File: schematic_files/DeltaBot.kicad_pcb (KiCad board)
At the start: 2 copper layers, 241.5 x 110.5 mm, 30 parts, among them J1 USB C PD Modulle, J2 LIDAR, J3 MOTOR_L, J4 MOTOR_R, SW1 SW_SPDT, U1 Radxa_ROCK5B, U2 Buck Converter

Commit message: Updated PCB layout
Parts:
- removed D1, D2: D, deltabot:D_DO-41_SOD81_P10.16mm_Horizontal
- removed REF** (x13), REF\: MountingHole_3.5mm, MountingHole:MountingHole_3.5mm
- J2: value LIDAR -> Conn_01x05; footprint deltabot:PinHeader_1x07_P2.54mm_Vertical -> Connector_PinHeader_2.54mm:PinHeader_1x05_P2.54mm_Vertical
- moved C1 191.3 mm to (40.5, 99.5)
- moved C2 176.7 mm to (43.2, 87.0), turned to 0 degrees
- moved U2 146.3 mm to (83.0, 100.5), turned to 180 degrees
- moved J2 5.07 mm to (171.1, 60.5)
- turned SW1 to 0 degrees
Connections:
- J2 pad 1: Net-(D2-K) -> unconnected-(J2-Pin_1-Pad1)
- J2 pad 2: MOTO_CTRL -> +5V
- J2 pad 3: GND -> LIDAR_TX
- J2 pad 4: +5V -> LIDAR_RX
- J2 pad 5: LIDAR_TX -> GND
- U1 pad 10: LIDAR_RX -> LIDAR_TX
- U1 pad 8: LIDAR_TX -> LIDAR_RX
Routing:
- net MOTO_CTRL: track 99.9 -> 0.00 mm, vias 1 -> 0
- net +5V: track 329.1 -> 380.8 mm
- net +9V: track 65.3 -> 113.4 mm
- net Net-(D2-K): track 35.8 -> 0.00 mm
- net LIDAR_TX: track 128.5 -> 105.5 mm
- net PWM_L: track 124.7 -> 140.5 mm
- net GND: track 11.4 -> 0.00 mm
- net Net-(D1-K): track 5.92 -> 0.00 mm
- net LIDAR_RX: track 112.6 -> 115.9 mm
- net Net-(SW1-B): track 72.0 -> 72.6 mm

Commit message: Small changes
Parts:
- moved J2 2.50 mm to (168.6, 60.5)
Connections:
- J2 pad 1: unconnected-(J2-Pin_1-Pad1) -> +5V
- J2 pad 2: +5V -> LIDAR_TX
- J2 pad 3: LIDAR_TX -> LIDAR_RX
- J2 pad 4: LIDAR_RX -> GND
- J2 pad 5: GND -> unconnected-(J2-Pin_5-Pad5)
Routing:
- net +5V: track 380.8 -> 375.9 mm
- net LIDAR_RX: track 115.9 -> 116.4 mm
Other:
- board text removed: "LIDAR_RX"
- board text removed: "LIDAR_TX"
- board text removed: "MOTOR_CTRL"
- board text removed: "PWM_R"
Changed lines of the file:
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@@
 	(net 34 "unconnected-(U1-GPIO2_B3-Pad7)")
 	(net 35 "PWM_R")
-	(net 36 "unconnected-(J2-Pin_1-Pad1)")
+	(net 36 "unconnected-(J2-Pin_5-Pad5)")
 	(net 37 "+9V")
 	(footprint "deltabot:C_Disc_D3.0mm_W2.0mm_P2.50mm"
@@
 			)
 		)
-		(group ""
-			(members "633756a8-9496-4de9-8571-4000073fd013" "c9b2ae1b-2e5a-42f9-9f94-d1d775f59a72")
-		)
 		(embedded_fonts no)
 	)
 	(footprint "Connector_PinHeader_2.54mm:PinHeader_1x05_P2.54mm_Vertical"
 		(layer "F.Cu")
-		(at 171.08 60.5 -90)
+		(at 168.58 60.5 -90)
 		(descr "Through hole straight pin header, 1x05, 2.54mm pitch, single row")
 		(tags "Through hole pin header THT 1x05 2.54mm single row")
@@
 			(layers "*.Cu" "*.Mask")
 			(remove_unused_layers no)
-			(net 36 "unconnected-(J2-Pin_1-Pad1)")
+			(net 26 "+5V")
 			(pinfunction "Pin_1")
 			(pintype "passive")
@@
 			(layers "*.Cu" "*.Mask")
 			(remove_unused_layers no)
-			(net 26 "+5V")
+			(net 10 "LIDAR_TX")
 			(pinfunction "Pin_2")
 			(pintype "passive")
@@
 			(layers "*.Cu" "*.Mask")
 			(remove_unused_layers no)
-			(net 10 "LIDAR_TX")
+			(net 27 "LIDAR_RX")
 			(pinfunction "Pin_3")
 			(pintype "passive")
@@
 			(layers "*.Cu" "*.Mask")
 			(remove_unused_layers no)
-			(net 27 "LIDAR_RX")
+			(net 1 "GND")
 			(pinfunction "Pin_4")
 			(pintype "passive")
@@
 			(layers "*.Cu" "*.Mask")
 			(remove_unused_layers no)
-			(net 1 "GND")
+			(net 36 "unconnected-(J2-Pin_5-Pad5)")
 			(pinfunction "Pin_5")
 			(pintype "passive")
@@
 		)
 	)
-	(gr_text "LIDAR_TX\n"
-		(at 114 45 0)
-		(layer "User.4")
-		(effects
-			(font
-				(size 1.5 1.5)
-				(thickness 0.3)
-				(bold yes)
-			)
-			(justify left bottom)
-		)
-	)
-	(gr_text "LIDAR_RX\n"
-		(at 114 55 0)
-		(layer "User.4")
-		(effects
-			(font
-				(size 1.5 1.5)
-				(thickness 0.3)
-				(bold yes)
-			)
-			(justify left bottom)
-		)
-	)
-	(gr_text "MOTOR_CTRL\n"
-		(at 114 66 0)
-		(layer "User.4")
-		(effects
-			(font
-				(size 1.5 1.5)
-				(thickness 0.3)
-				(bold yes)
-			)
-			(justify left bottom)
-		)
-	)
 	(gr_text "+9V"
 		(at 170 114 0)
@@
 		)
 	)
-	(gr_text "PWM_R"
-		(at 114 69 0)
-		(layer "User.8")
-		(effects
-			(font
-				(size 1.5 1.5)
-				(thickness 0.3)
-				(bold yes)
-			)
-			(justify left bottom)
-		)
-	)
 	(gr_text "PWM_L\n"
 		(at 132.5 110 0)
@@
 	)
 	(via
-		(at 156 60)
+		(at 153.5 60.5)
 		(size 2.5)
 		(drill 1)
@@
 	)
 	(via
-		(at 179.5 58)
+		(at 180 55)
 		(size 2.5)
 		(drill 1)
@@
 	)
 	(via
-		(at 77 68)
+		(at 77 69.5)
 		(size 2.5)
 		(drill 1)
@@
 	)
 	(via
-		(at 96.5 79.5)
+		(at 92.5 79.5)
 		(size 2.5)
 		(drill 1)
@@
 	)
 	(segment
+		(start 166.04 60.5)
+		(end 166 60.5)
+		(width 0.5)
+		(layer "B.Cu")
+		(net 10)
+	)
+	(segment
 		(start 166 63.5)
 		(end 166 60.5)
@@
 	)
 	(segment
-		(start 58.5 60)
-		(end 58.5 55)
-		(width 1)
+		(start 186.5 40.5)
+		(end 201 55)
+		(width 2.5)
 		(layer "B.Cu")
 		(net 26)
 	)
 	(segment
-		(start 186.5 40.5)
-		(end 201 55)
-		(width 2.5)
+		(start 168.58 60.5)
+		(end 168.58 60.075)
+		(width 0.5)
 		(layer "B.Cu")
 		(net 26)
 	)
 	(segment
-		(start 209 62)
-		(end 209 114.5)
-		(width 2)
+		(start 168.58 60.075)
+		(end 168.505 60)
+		(width 0.5)
 		(layer "B.Cu")
 		(net 26)
 	)
 	(segment
-		(start 60 53.5)
-		(end 64 53.5)
-		(width 1)
+		(start 209 62)
+		(end 209 114.5)
+		(width 2)
 		(layer "B.Cu")
 		(net 26)
@@
 	)
 	(segment
+		(start 58.5 60)
+		(end 63.5 60)
+		(width 1)
+		(layer "B.Cu")
+		(net 26)
+	)
+	(segment
 		(start 207.04 63.96)
 		(end 205.25 63.96)
@@
 	)
 	(segment
-		(start 58.5 55)
-		(end 60 53.5)
-		(width 1)
-		(layer "B.Cu")
-		(net 26)
-	)
-	(segment
 		(start 209 114.5)
 		(end 206.46 117.04)
@@
 	)
 	(segment
+		(start 63.5 60)
+		(end 64 59.5)
+		(width 1)
+		(layer "B.Cu")
+		(net 26)
+	)
+	(segment
 		(start 202.75 71.75)
 		(end 205.25 69.25)
@@
 	)
 	(segment
-		(start 124.5 59.5)
-		(end 130 54)
+		(start 130 54)
+		(end 163.5 54)
 		(width 1)
 		(layer "B.Cu")
@@
 	)
 	(segment
-		(start 163.5 54)
-		(end 163.5 60)
+		(start 124.5 59.5)
+		(end 130 54)
 		(width 1)
 		(layer "B.Cu")
@@
 	)
 	(segment
-		(start 130 54)
-		(end 163.5 54)
+		(start 163.5 54)
+		(end 163.5 60.5)
 		(width 1)
 		(layer "B.Cu")

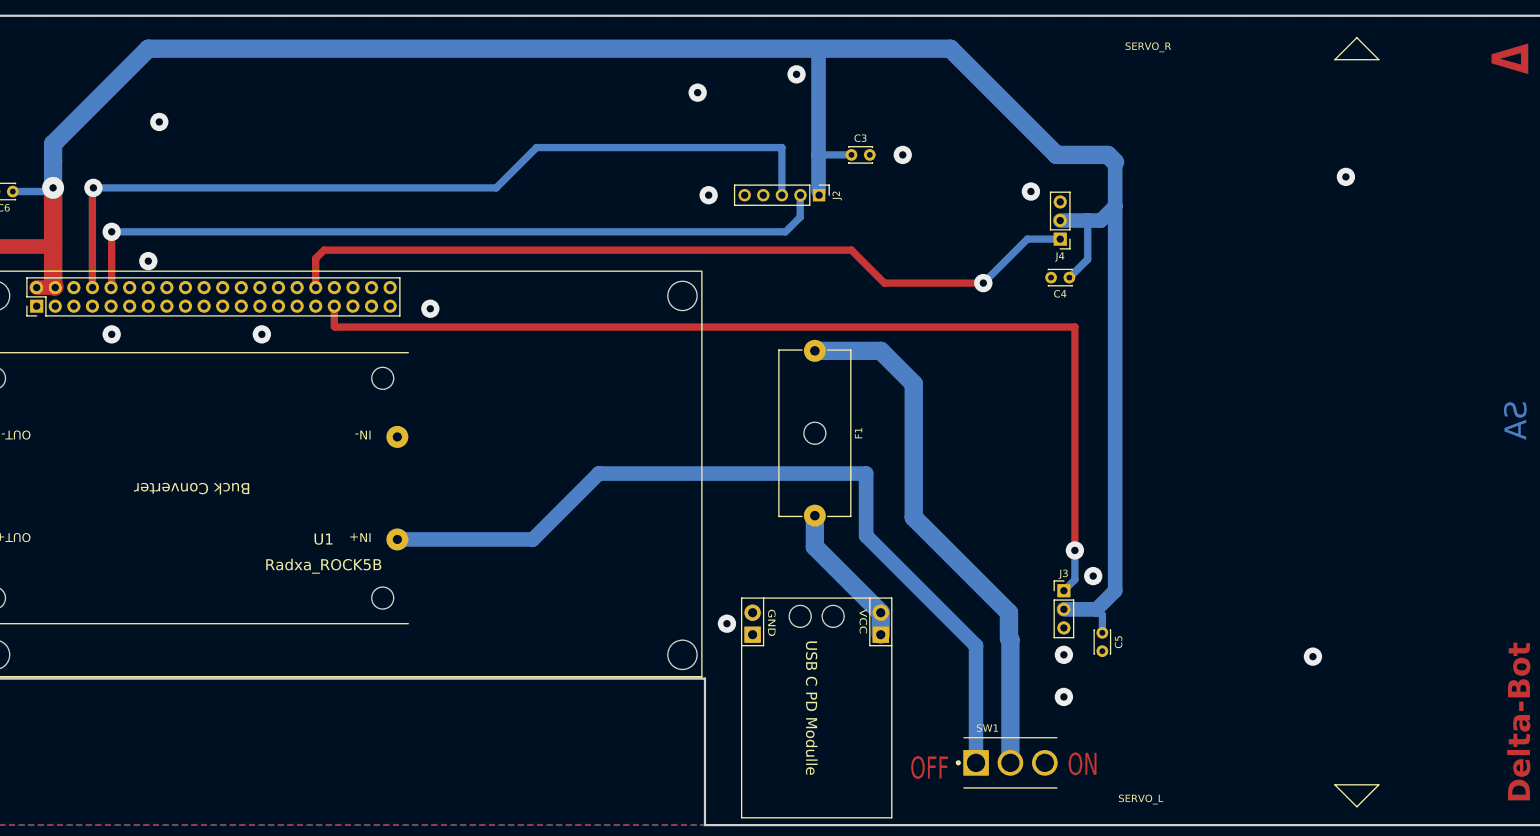
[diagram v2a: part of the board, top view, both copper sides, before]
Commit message: Added C1 LIDAR to the footprints.
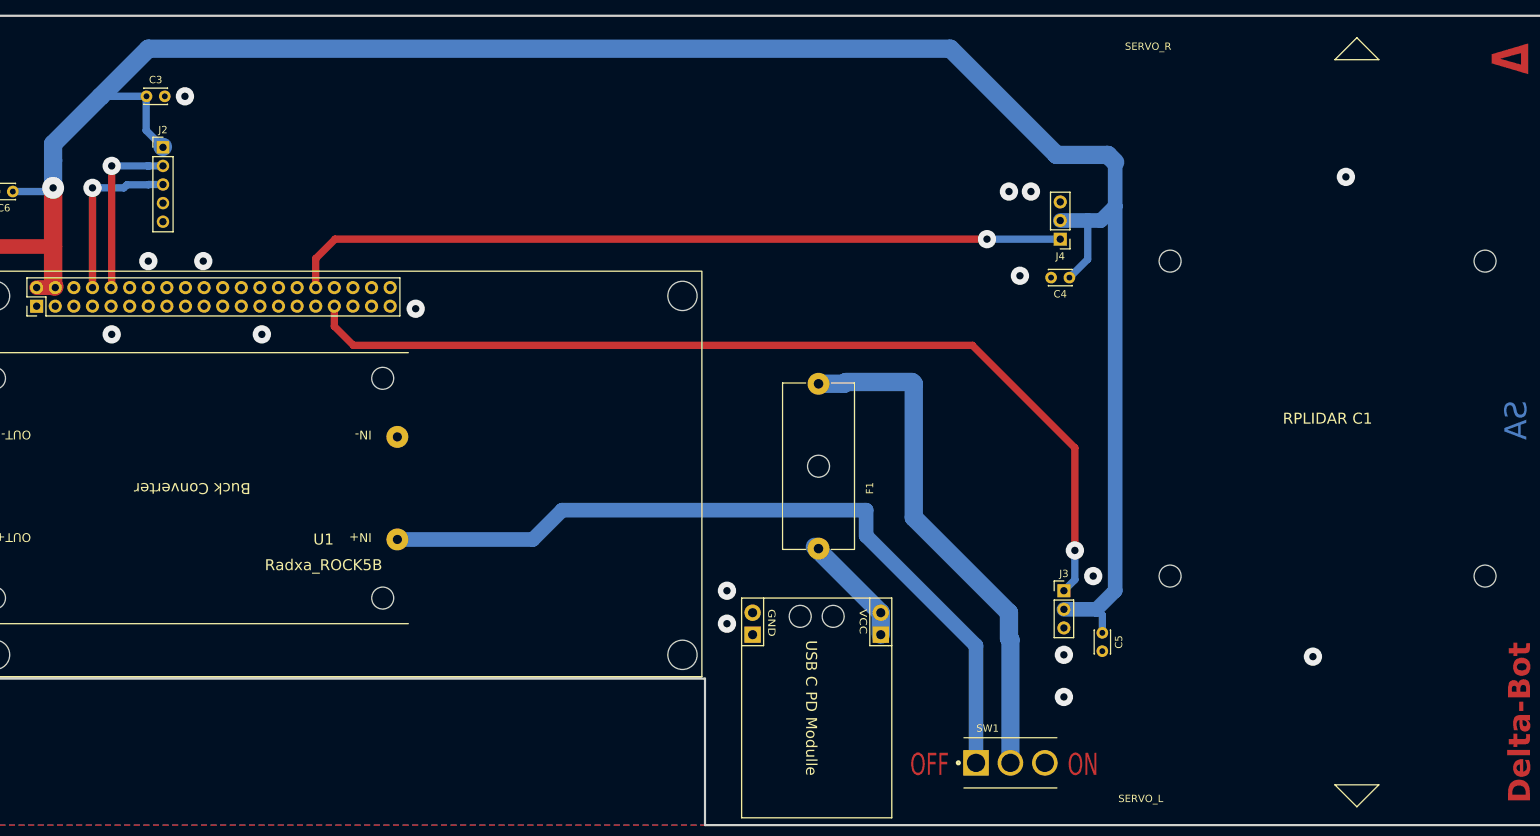
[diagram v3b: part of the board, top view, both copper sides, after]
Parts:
- added U1: RPLIDAR C1, deltabot:RPLIDAR C1, F.Cu at (238.0, 91.0)
- J2: value Conn_01x05 -> LIDAR
- moved C3 96.6 mm to (76.8, 47.0)
- moved J2 89.8 mm to (79.0, 54.0), turned to 0 degrees
- moved F1 4.53 mm to (168.5, 86.2)
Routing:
- net LIDAR_RX: track 116.4 -> 23.4 mm
- net LIDAR_TX: track 105.5 -> 23.7 mm
- net PWM_L: track 140.5 -> 130.8 mm
- net +5V: track 375.9 -> 366.3 mm
- net +9V: track 113.4 -> 106.4 mm
- net Net-(J1-VCC): track 20.0 -> 15.7 mm
- net PWM_R: track 110.4 -> 106.7 mm
- net Net-(SW1-B): track 72.6 -> 70.4 mm
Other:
- board text removed: "+5V"
- board text removed: "+8.34V"
- board text removed: "+9V"
- board text removed: "PWM_L"

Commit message: Fixed the Rock5B footprint which was slightly off.
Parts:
- moved U1 0.84 mm to (101.8, 109.0)
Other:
- outline, holes or cut-outs redrawn

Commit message: Added files for GU manufacture
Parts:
- moved C5 8.61 mm to (199.5, 124.0), turned to 0 degrees
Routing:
- net +5V: track 366.3 -> 372.2 mm
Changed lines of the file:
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@@
 		(1 "F.Mask" user)
 		(3 "B.Mask" user)
-		(17 "Dwgs.User" user "User.Drawings")
-		(19 "Cmts.User" user "User.Comments")
-		(21 "Eco1.User" user "User.Eco1")
-		(23 "Eco2.User" user "User.Eco2")
 		(25 "Edge.Cuts" user)
 		(27 "Margin" user)
@@
 		(35 "F.Fab" user)
 		(33 "B.Fab" user)
-		(39 "User.1" user)
-		(41 "User.2" user)
-		(43 "User.3" user)
-		(45 "User.4" user)
-		(47 "User.5" user)
-		(49 "User.6" user)
-		(51 "User.7" user)
-		(53 "User.8" user)
-		(55 "User.9" user)
 	)
 	(setup
+		(stackup
+			(layer "F.SilkS"
+				(type "Top Silk Screen")
+			)
+			(layer "F.Paste"
+				(type "Top Solder Paste")
+			)
+			(layer "F.Mask"
+				(type "Top Solder Mask")
+				(thickness 0.01)
+			)
+			(layer "F.Cu"
+				(type "copper")
+				(thickness 0.035)
+			)
+			(layer "dielectric 1"
+				(type "core")
+				(thickness 1.51)
+				(material "FR4")
+				(epsilon_r 4.5)
+				(loss_tangent 0.02)
+			)
+			(layer "B.Cu"
+				(type "copper")
+				(thickness 0.035)
+			)
+			(layer "B.Mask"
+				(type "Bottom Solder Mask")
+				(thickness 0.01)
+			)
+			(layer "B.Paste"
+				(type "Bottom Solder Paste")
+			)
+			(layer "B.SilkS"
+				(type "Bottom Silk Screen")
+			)
+			(copper_finish "None")
+			(dielectric_constraints no)
+		)
 		(pad_to_mask_clearance 0)
 		(allow_soldermask_bridges_in_footprints no)
@@
 			(drillshape 0)
 			(scaleselection 1)
-			(outputdirectory "../../pcb svg/new schem & pcb/")
+			(outputdirectory "/tmp/drill")
 		)
 	)
@@
 	(footprint "deltabot:C_Disc_D3.0mm_W2.0mm_P2.50mm"
 		(layer "F.Cu")
-		(at 207.25 120.25 -90)
+		(at 199.5 124)
 		(descr "C, Disc series, Radial, pin pitch=2.50mm, , diameter*width=3*2mm^2, Capacitor")
 		(tags "C Disc series Radial pin pitch 2.50mm  diameter 3mm width 2mm Capacitor")
 		(property "Reference" "C5"
-			(at 1.25 -2.25 90)
+			(at 1.25 -2.25 0)
 			(layer "F.SilkS")
 			(effects
@@
 		)
 		(property "Value" "1uF"
-			(at 1.25 2.25 90)
+			(at 1.25 2.25 0)
 			(layer "F.Fab")
 			(effects
@@
 		)
 		(property "Datasheet" "~"
-			(at 0 0 270)
+			(at 0 0 0)
 			(unlocked yes)
 			(layer "F.Fab")
@@
 		)
 		(property "Description" "Polarized capacitor"
-			(at 0 0 270)
+			(at 0 0 0)
 			(unlocked yes)
 			(layer "F.Fab")
@@
 		(attr through_hole)
 		(fp_line
-			(start -0.37 1.12)
-			(end 2.87 1.12)
+			(start -0.37 -1.12)
+			(end -0.37 -1.055)
 			(stroke
 				(width 0.12)
@@
 		)
 		(fp_line
-			(start -0.37 1.055)
-			(end -0.37 1.12)
+			(start -0.37 -1.12)
+			(end 2.87 -1.12)
 			(stroke
 				(width 0.12)
@@
 		)
 		(fp_line
-			(start 2.87 1.055)
-			(end 2.87 1.12)
+			(start -0.37 1.055)
+			(end -0.37 1.12)
 			(stroke
 				(width 0.12)
@@
 		)
 		(fp_line
-			(start -0.37 -1.12)
-			(end -0.37 -1.055)
+			(start -0.37 1.12)
+			(end 2.87 1.12)
 			(stroke
 				(width 0.12)
@@
 		)
 		(fp_line
-			(start -0.37 -1.12)
-			(end 2.87 -1.12)
+			(start 2.87 -1.12)
+			(end 2.87 -1.055)
 			(stroke
 				(width 0.12)
@@
 		)
 		(fp_line
-			(start 2.87 -1.12)
-			(end 2.87 -1.055)
+			(start 2.87 1.055)
+			(end 2.87 1.12)
 			(stroke
 				(width 0.12)
@@
 		)
 		(fp_line
-			(start -1.05 1.25)
-			(end 3.55 1.25)
+			(start -1.05 -1.25)
+			(end -1.05 1.25)
 			(stroke
 				(width 0.05)
@@
 		)
 		(fp_line
-			(start 3.55 1.25)
-			(end 3.55 -1.25)
+			(start -1.05 1.25)
+			(end 3.55 1.25)
 			(stroke
 				(width 0.05)
@@
 		)
 		(fp_line
-			(start -1.05 -1.25)
-			(end -1.05 1.25)
+			(start 3.55 -1.25)
+			(end -1.05 -1.25)
 			(stroke
 				(width 0.05)
@@
 		)
 		(fp_line
-			(start 3.55 -1.25)
-			(end -1.05 -1.25)
+			(start 3.55 1.25)
+			(end 3.55 -1.25)
 			(stroke
 				(width 0.05)
@@
 		)
 		(fp_line
-			(start -0.25 1)
-			(end 2.75 1)
+			(start -0.25 -1)
+			(end -0.25 1)
 			(stroke
 				(width 0.1)
@@
 		)
 		(fp_line
-			(start 2.75 1)
-			(end 2.75 -1)
+			(start -0.25 1)
+			(end 2.75 1)
 			(stroke
 				(width 0.1)
@@
 		)
 		(fp_line
-			(start -0.25 -1)
-			(end -0.25 1)
+			(start 2.75 -1)
+			(end -0.25 -1)
 			(stroke
 				(width 0.1)
@@
 		)
 		(fp_line
-			(start 2.75 -1)
-			(end -0.25 -1)
+			(start 2.75 1)
+			(end 2.75 -1)
 			(stroke
 				(width 0.1)
@@
 		)
 		(fp_text user "${REFERENCE}"
-			(at 1.25 0 90)
+			(at 1.25 0 0)
 			(layer "F.Fab")
 			(effects
@@
 		)
 		(pad "1" thru_hole circle
-			(at 0 0 270)
+			(at 0 0)
 			(size 1.6 1.6)
 			(drill 0.8)
@@
 		)
 		(pad "2" thru_hole circle
-			(at 2.5 0 270)
+			(at 2.5 0)
 			(size 1.6 1.6)
 			(drill 0.8)
@@
 	)
 	(gr_line
-		(start 208.5 50.5)
-		(end 208.5 37)
-		(stroke
-			(width 0.12)
-			(type solid)
-		)
-		(layer "Cmts.User")
-	)
-	(gr_line
-		(start 208.5 50.5)
-		(end 248.5 50.5)
-		(stroke
-			(width 0.12)
-			(type solid)
-		)
-		(layer "Cmts.User")
-	)
-	(gr_line
-		(start 208.5 132.5)
-		(end 208.5 145.5)
-		(stroke
-			(width 0.12)
-			(type solid)
-		)
-		(layer "Cmts.User")
-	)
-	(gr_line
-		(start 248.5 50.5)
-		(end 248.5 37)
-		(stroke
-			(width 0.12)
-			(type solid)
-		)
-		(layer "Cmts.User")
-	)
-	(gr_line
-		(start 248.5 132.5)
-		(end 208.5 132.5)
-		(stroke
-			(width 0.12)
-			(type solid)
-		)
-		(layer "Cmts.User")
-	)
-	(gr_line
-		(start 248.5 132.5)
-		(end 248.5 145.5)
-		(stroke
-			(width 0.12)
-			(type solid)
-		)
-		(layer "Cmts.User")
-	)
-	(gr_line
 		(start 27 36)
 		(end 268.5 36)
@@
 		)
 	)
-	(gr_text "\n"
-		(at 208 97.5 0)
-		(layer "Cmts.User")
-		(effects
-			(font
-				(size 1.5 1.5)
-				(thickness 0.3)
-				(bold yes)
-			)
-			(justify left bottom)
-		)
-	)
 	(via
 		(at 110 78.5)
@@
 	)
 	(via
-		(at 236 123.5)
+		(at 205.5 120)
 		(size 2.5)
 		(drill 1)
@@
 	)
 	(via
-		(at 202 123.25)
+		(at 217 135.5)
 		(size 2.5)
 		(drill 1)
@@
 		(start 40.5 99.5)
 		(end 40.5 87)
-		(width 2)
+		(width 2.5)
+		(layer "F.Cu")
+		(net 26)
+	)
+	(segment
+		(start 199.5 117)
+		(end 200.5 117)
+		(width 1)
 		(layer "F.Cu")
 		(net 26)
@@
 		(start 40.5 99.5)
 		(end 40.5 107.5)
-		(width 2)
+		(width 2.5)
 		(layer "F.Cu")
 		(net 26)
 	)
 	(segment
-		(start 40.5 67.5)
+		(start 62 67.5)
 		(end 64 67.5)
-		(width 2)
+		(width 2.5)
 		(layer "F.Cu")
 		(net 26)
@@
 		(start 40.5 87)
 		(end 40.5 67.5)
-		(width 2)
+		(width 2.5)
 		(layer "F.Cu")
 		(net 26)
 	)
 	(segment
-		(start 64 72.82)
-		(end 64.185 73.005)
-		(width 2.5)
+		(start 200.5 117)
+		(end 200.54 117.04)
+		(width 1)
 		(layer "F.Cu")
 		(net 26)
 	)
 	(segment
-		(start 64 67.5)
-		(end 64 72.82)
-		(width 2.5)
+		(start 61.8 67.7)
+		(end 62 67.5)
+		(width 1.8)
+		(layer "F.Cu")
+		(net 26)
+	)
+	(segment
+		(start 64.34 72.96)
+		(end 61.8 72.96)
+		(width 1.8)
 		(layer "F.Cu")
 		(net 26)
@@
 	)
 	(segment
-		(start 64.295 73.115)
-		(end 61.755 73.115)
-		(width 2)
+		(start 40.5 67.5)
+		(end 62 67.5)
+		(width 2.5)
+		(layer "F.Cu")
+		(net 26)
+	)
+	(segment
+		(start 61.8 72.96)
+		(end 61.8 67.7)
+		(width 1.8)
+		(layer "F.Cu")
+		(net 26)
+	)
+	(segment
+		(start 199.5 124)
+		(end 199.5 117)
+		(width 1)
+		(layer "F.Cu")
+		(net 26)
+	)
+	(segment
+		(start 200.54 117.04)
+		(end 202 117.04)
+		(width 1)
 		(layer "F.Cu")
 		(net 26)
@@
 		(start 54 107.5)
 		(end 40.5 107.5)
-		(width 2)
+		(width 2.5)
 		(layer "F.Cu")
 		(net 26)
@@
 	)
 	(segment
-		(start 207.25 117.83)
-		(end 206.46 117.04)
-		(width 1)
-		(layer "B.Cu")
-		(net 26)
-	)
-	(segment
 		(start 58.5 60.25)
 		(end 58.5 60)
@@
 	)
 	(segment
-		(start 207.25 120.25)
-		(end 207.25 117.83)
-		(width 1)
-		(layer "B.Cu")
-		(net 26)
-	)
-	(segment
 		(start 209 62)
 		(end 207.04 63.96)
@@
 		)
 	)
-	(group ""
-		(members "c2809287-a368-40c3-bb0e-89477e0ef6f8")
-	)
 	(embedded_fonts no)
